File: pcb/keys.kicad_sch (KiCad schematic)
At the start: 58 parts, among them SW1 SW_Push

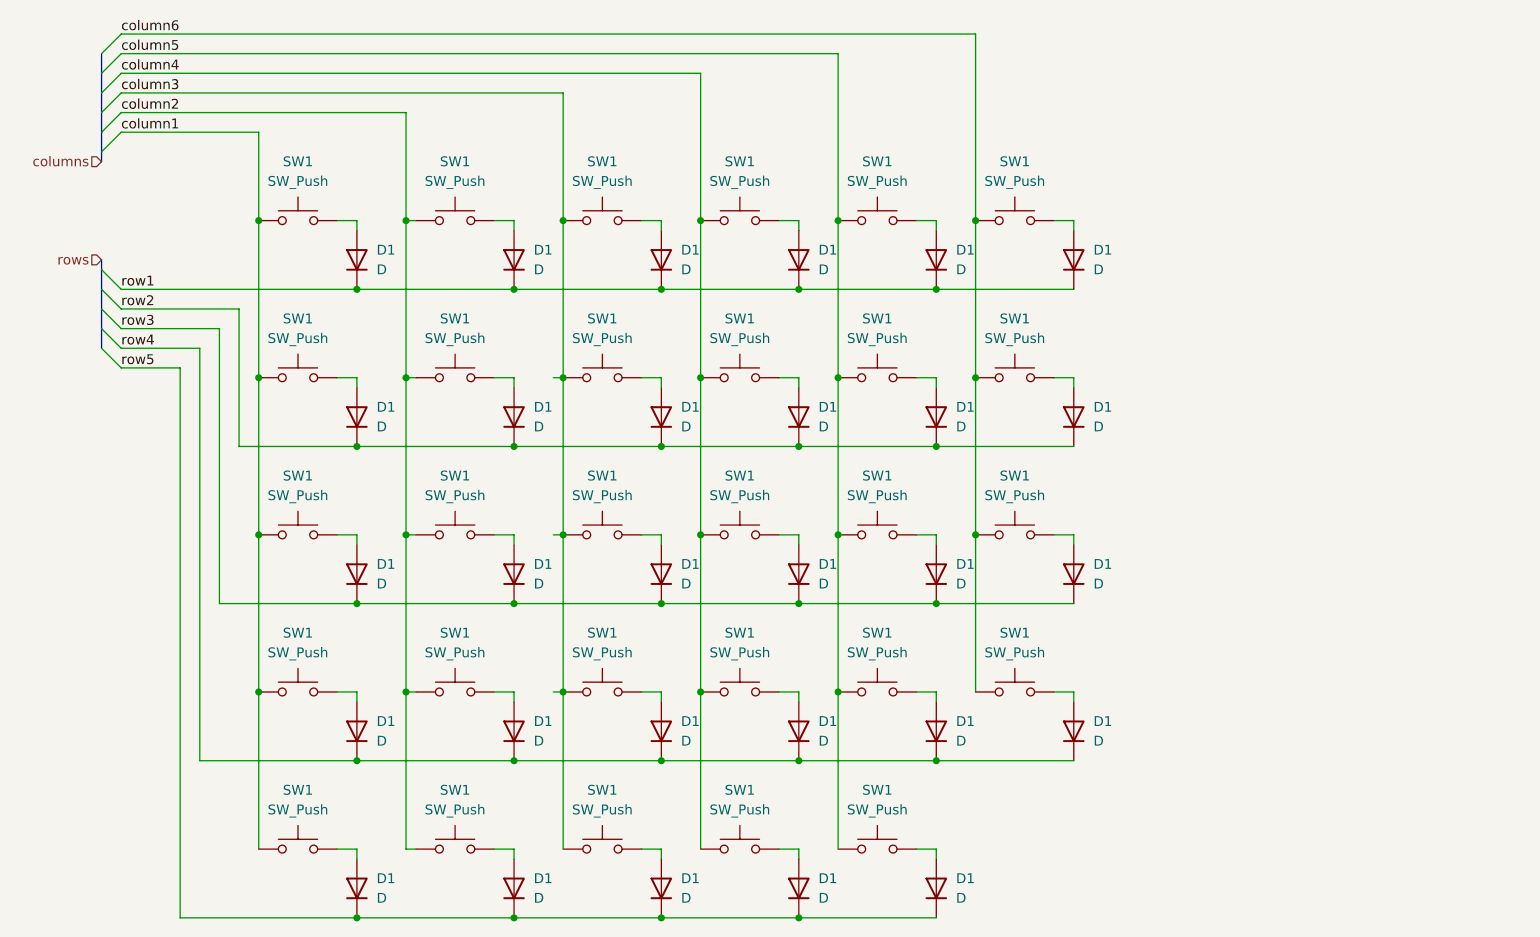
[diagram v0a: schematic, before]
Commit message: USB 3.1 Type C com PD configurado
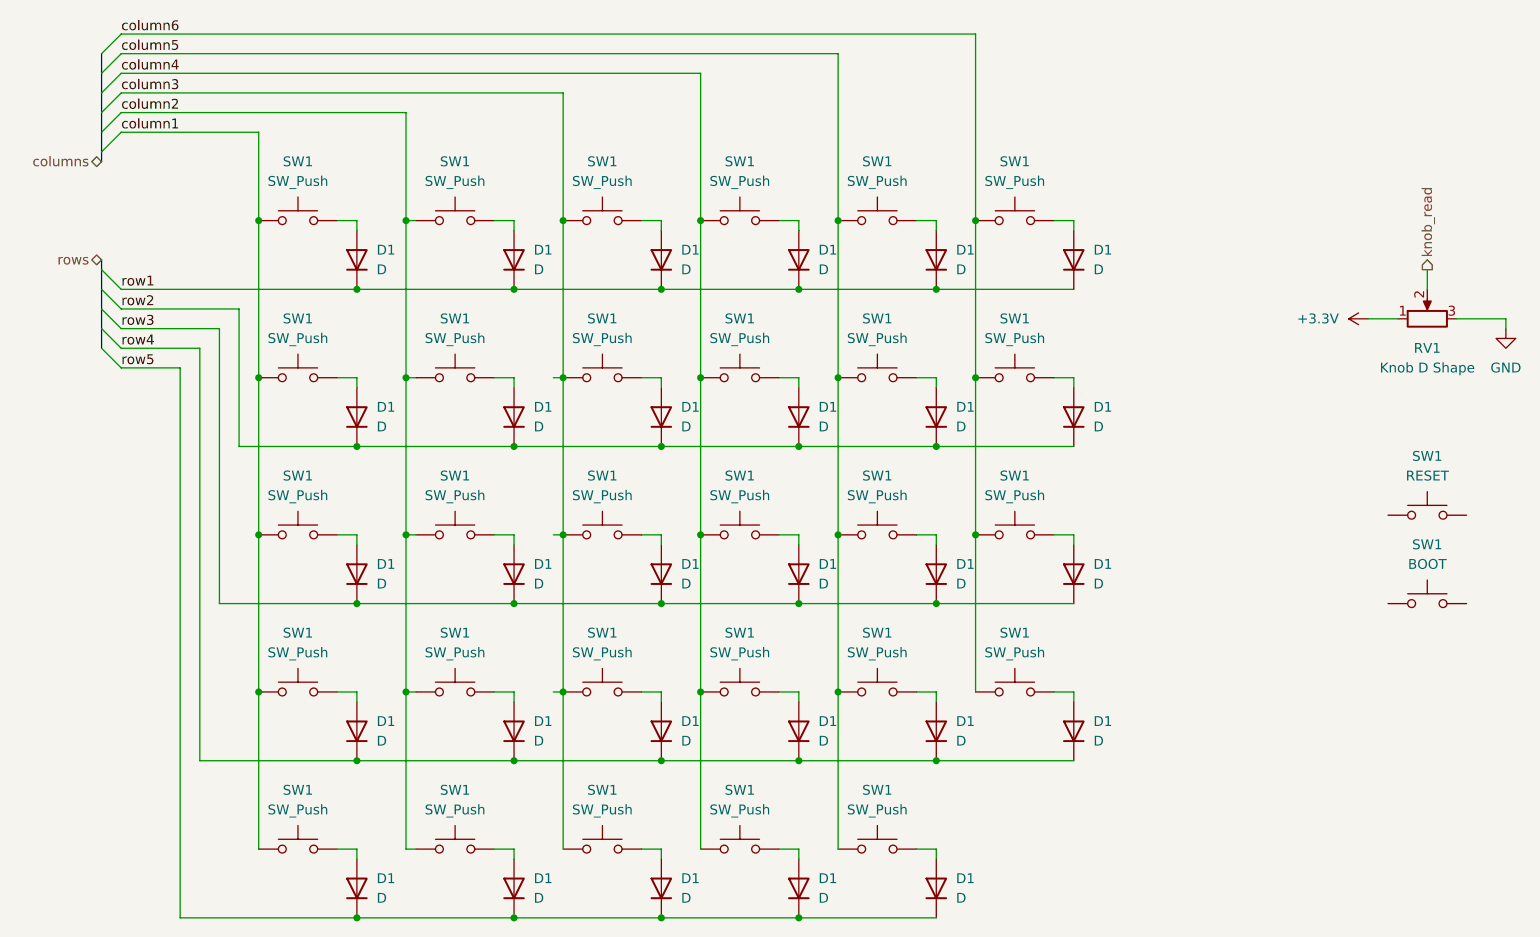
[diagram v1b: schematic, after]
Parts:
- added RV1: Knob D Shape, symbol Device:R_Potentiometer
- added SW1: BOOT, symbol Switch:SW_Push
- added SW1: RESET, symbol Switch:SW_Push
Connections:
- new net +3.3V: RV1.1
- new net GND: RV1.3
- new net knob_read: RV1.2
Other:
- title: (none) -> バングー Keyboard Schematic
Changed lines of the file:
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@@
 (kicad_sch (version 20230121) (generator eeschema)
   (paper "A4")
+  (title_block
+    (title "バングー Keyboard Schematic")
+    (date "2024-01-20")
+  )
   (junction (at 133.35 57.15) (diameter 0) (color 0 0 0 0)
   )
@@
     (stroke (width 0) (type default))
   )
+  (wire (pts (xy 248.92 69.85) (xy 255.27 69.85))
+    (stroke (width 0) (type default))
+  )
   (wire (pts (xy 163.83 147.32) (xy 181.61 147.32))
     (stroke (width 0) (type default))
@@
     (stroke (width 0) (type default))
   )
+  (wire (pts (xy 255.27 69.85) (xy 255.27 71.12))
+    (stroke (width 0) (type default))
+  )
   (wire (pts (xy 106.68 86.36) (xy 127 86.36))
     (stroke (width 0) (type default))
@@
     (stroke (width 0) (type default))
   )
+  (wire (pts (xy 237.49 69.85) (xy 241.3 69.85))
+    (stroke (width 0) (type default))
+  )
   (wire (pts (xy 104.14 57.15) (xy 106.68 57.15))
     (stroke (width 0) (type default))
@@
   )
   (wire (pts (xy 127 86.36) (xy 146.05 86.36))
+    (stroke (width 0) (type default))
+  )
+  (wire (pts (xy 245.11 63.5) (xy 245.11 66.04))
     (stroke (width 0) (type default))
   )
@@
     (effects (font (size 1.27 1.27)) (justify left bottom))
   )
-  (hierarchical_label "rows" (shape input) (at 73.66 62.23 180) (fields_autoplaced)
+  (hierarchical_label "rows" (shape bidirectional) (at 73.66 62.23 180) (fields_autoplaced)
     (effects (font (size 1.27 1.27)) (justify right))
   )
-  (hierarchical_label "columns" (shape input) (at 73.66 49.53 180) (fields_autoplaced)
+  (hierarchical_label "knob_read" (shape output) (at 245.11 63.5 90) (fields_autoplaced)
+    (effects (font (size 1.27 1.27)) (justify left))
+  )
+  (hierarchical_label "columns" (shape bidirectional) (at 73.66 49.53 180) (fields_autoplaced)
     (effects (font (size 1.27 1.27)) (justify right))
   )
@@
     )
   )
+  (symbol (lib_id "Device:R_Potentiometer") (at 245.11 69.85 90) (unit 1)
+    (in_bom yes) (on_board yes) (dnp no) (fields_autoplaced)
+    (property "Reference" "RV1" (at 245.11 73.66 90)
+      (effects (font (size 1.27 1.27)))
+    )
+    (property "Value" "Knob D Shape" (at 245.11 76.2 90)
+      (effects (font (size 1.27 1.27)))
+    )
+    (property "Footprint" "" (at 245.11 69.85 0)
+      (effects (font (size 1.27 1.27)) hide)
+    )
+    (property "Datasheet" "~" (at 245.11 69.85 0)
+      (effects (font (size 1.27 1.27)) hide)
+    )
+    (pin "2")
+    (pin "1")
+    (pin "3")
+    (instances
+      (project "lily58_keyboard"
+        (path "/e186517a-3325-4e77-9fb6-41adae966a58/f4872a4f-f030-46a7-afd5-727446dac0a1"
+          (reference "RV1") (unit 1)
+        )
+      )
+    )
+  )
+  (symbol (lib_id "power:+3.3V") (at 237.49 69.85 90) (unit 1)
+    (in_bom yes) (on_board yes) (dnp no) (fields_autoplaced)
+    (property "Reference" "#PWR06" (at 241.3 69.85 0)
+      (effects (font (size 1.27 1.27)) hide)
+    )
+    (property "Value" "+3.3V" (at 233.68 69.85 90)
+      (effects (font (size 1.27 1.27)) (justify left))
+    )
+    (property "Footprint" "" (at 237.49 69.85 0)
+      (effects (font (size 1.27 1.27)) hide)
+    )
+    (property "Datasheet" "" (at 237.49 69.85 0)
+      (effects (font (size 1.27 1.27)) hide)
+    )
+    (pin "1")
+    (instances
+      (project "lily58_keyboard"
+        (path "/e186517a-3325-4e77-9fb6-41adae966a58/f4872a4f-f030-46a7-afd5-727446dac0a1"
+          (reference "#PWR06") (unit 1)
+        )
+      )
+    )
+  )
   (symbol (lib_id "Switch:SW_Push") (at 138.43 97.79 0) (unit 1)
     (in_bom yes) (on_board yes) (dnp no) (fields_autoplaced)
@@
     )
   )
+  (symbol (lib_id "Switch:SW_Push") (at 245.11 106.68 0) (unit 1)
+    (in_bom yes) (on_board yes) (dnp no) (fields_autoplaced)
+    (property "Reference" "SW1" (at 245.11 99.06 0)
+      (effects (font (size 1.27 1.27)))
+    )
+    (property "Value" "BOOT" (at 245.11 101.6 0)
+      (effects (font (size 1.27 1.27)))
+    )
+    (property "Footprint" "" (at 245.11 101.6 0)
+      (effects (font (size 1.27 1.27)) hide)
+    )
+    (property "Datasheet" "~" (at 245.11 101.6 0)
+      (effects (font (size 1.27 1.27)) hide)
+    )
+    (pin "2")
+    (pin "1")
+    (instances
+      (project "lily58_keyboard"
+        (path "/e186517a-3325-4e77-9fb6-41adae966a58"
+          (reference "SW1") (unit 1)
+        )
+        (path "/e186517a-3325-4e77-9fb6-41adae966a58/f4872a4f-f030-46a7-afd5-727446dac0a1"
+          (reference "SW31") (unit 1)
+        )
+      )
+    )
+  )
   (symbol (lib_id "Switch:SW_Push") (at 119.38 97.79 0) (unit 1)
     (in_bom yes) (on_board yes) (dnp no) (fields_autoplaced)
@@
     )
   )
+  (symbol (lib_id "power:GND") (at 255.27 71.12 0) (unit 1)
+    (in_bom yes) (on_board yes) (dnp no) (fields_autoplaced)
+    (property "Reference" "#PWR05" (at 255.27 77.47 0)
+      (effects (font (size 1.27 1.27)) hide)
+    )
+    (property "Value" "GND" (at 255.27 76.2 0)
+      (effects (font (size 1.27 1.27)))
+    )
+    (property "Footprint" "" (at 255.27 71.12 0)
+      (effects (font (size 1.27 1.27)) hide)
+    )
+    (property "Datasheet" "" (at 255.27 71.12 0)
+      (effects (font (size 1.27 1.27)) hide)
+    )
+    (pin "1")
+    (instances
+      (project "lily58_keyboard"
+        (path "/e186517a-3325-4e77-9fb6-41adae966a58/f4872a4f-f030-46a7-afd5-727446dac0a1"
+          (reference "#PWR05") (unit 1)
+        )
+      )
+    )
+  )
   (symbol (lib_id "Device:D") (at 181.61 62.23 90) (unit 1)
     (in_bom yes) (on_board yes) (dnp no) (fields_autoplaced)
@@
         )
       )
+    )
+  )
+  (symbol (lib_id "Switch:SW_Push") (at 245.11 95.25 0) (unit 1)
+    (in_bom yes) (on_board yes) (dnp no) (fields_autoplaced)
+    (property "Reference" "SW1" (at 245.11 87.63 0)
+      (effects (font (size 1.27 1.27)))
+    )
+    (property "Value" "RESET" (at 245.11 90.17 0)
+      (effects (font (size 1.27 1.27)))
+    )
+    (property "Footprint" "" (at 245.11 90.17 0)
+      (effects (font (size 1.27 1.27)) hide)
+    )
+    (property "Datasheet" "~" (at 245.11 90.17 0)
+      (effects (font (size 1.27 1.27)) hide)
+    )
+    (pin "2")
+    (pin "1")
+    (instances
+      (project "lily58_keyboard"
+        (path "/e186517a-3325-4e77-9fb6-41adae966a58"
+          (reference "SW1") (unit 1)
+        )
+        (path "/e186517a-3325-4e77-9fb6-41adae966a58/f4872a4f-f030-46a7-afd5-727446dac0a1"
+          (reference "SW30") (unit 1)
+        )
+      )

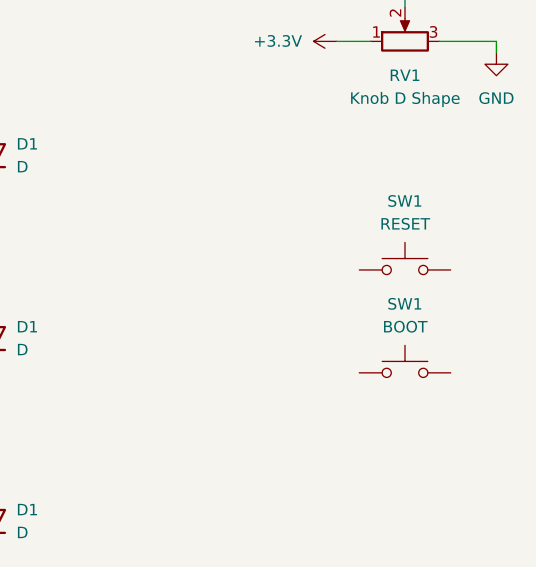
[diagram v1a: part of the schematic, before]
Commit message: trocando ESP-WROOM por ESP-S3 & removendo chaves de flash
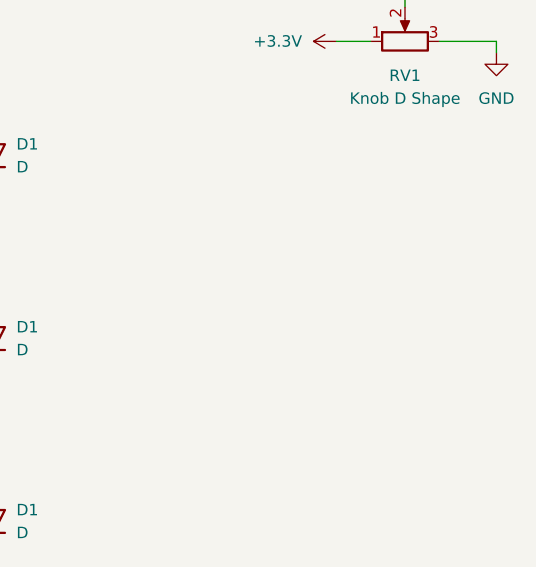
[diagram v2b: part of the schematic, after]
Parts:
- removed SW1: BOOT, symbol Switch:SW_Push
- removed SW1: RESET, symbol Switch:SW_Push
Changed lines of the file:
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@@
-    )
-  )
-  (symbol (lib_id "Switch:SW_Push") (at 245.11 106.68 0) (unit 1)
-    (in_bom yes) (on_board yes) (dnp no) (fields_autoplaced)
-    (property "Reference" "SW1" (at 245.11 99.06 0)
-      (effects (font (size 1.27 1.27)))
-    )
-    (property "Value" "BOOT" (at 245.11 101.6 0)
-      (effects (font (size 1.27 1.27)))
-    )
-    (property "Footprint" "" (at 245.11 101.6 0)
-      (effects (font (size 1.27 1.27)) hide)
-    )
-    (property "Datasheet" "~" (at 245.11 101.6 0)
-      (effects (font (size 1.27 1.27)) hide)
-    )
-    (pin "2")
-    (pin "1")
-    (instances
-      (project "lily58_keyboard"
-        (path "/e186517a-3325-4e77-9fb6-41adae966a58"
-          (reference "SW1") (unit 1)
-        )
-        (path "/e186517a-3325-4e77-9fb6-41adae966a58/f4872a4f-f030-46a7-afd5-727446dac0a1"
-          (reference "SW31") (unit 1)
-        )
-      )
     )
   )
@@
         )
       )
-    )
-  )
-  (symbol (lib_id "Switch:SW_Push") (at 245.11 95.25 0) (unit 1)
-    (in_bom yes) (on_board yes) (dnp no) (fields_autoplaced)
-    (property "Reference" "SW1" (at 245.11 87.63 0)
-      (effects (font (size 1.27 1.27)))
-    )
-    (property "Value" "RESET" (at 245.11 90.17 0)
-      (effects (font (size 1.27 1.27)))
-    )
-    (property "Footprint" "" (at 245.11 90.17 0)
-      (effects (font (size 1.27 1.27)) hide)
-    )
-    (property "Datasheet" "~" (at 245.11 90.17 0)
-      (effects (font (size 1.27 1.27)) hide)
-    )
-    (pin "2")
-    (pin "1")
-    (instances
-      (project "lily58_keyboard"
-        (path "/e186517a-3325-4e77-9fb6-41adae966a58"
-          (reference "SW1") (unit 1)
-        )
-        (path "/e186517a-3325-4e77-9fb6-41adae966a58/f4872a4f-f030-46a7-afd5-727446dac0a1"
-          (reference "SW30") (unit 1)
-        )
-      )
